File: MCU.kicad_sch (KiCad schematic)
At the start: 47 parts, among them J1 USB_C_Receptacle_USB2.0_16P, J2 DE9_Pins_MountingHoles, Q1 BC817, Q2 BC817, Q3 BC817, Q4 BC817, SW1 SW_SPST, SW2 SW_SPST, U1 W25Q128JVS, U2 ESP32-S3-MINI-1U, U3 MAX3232

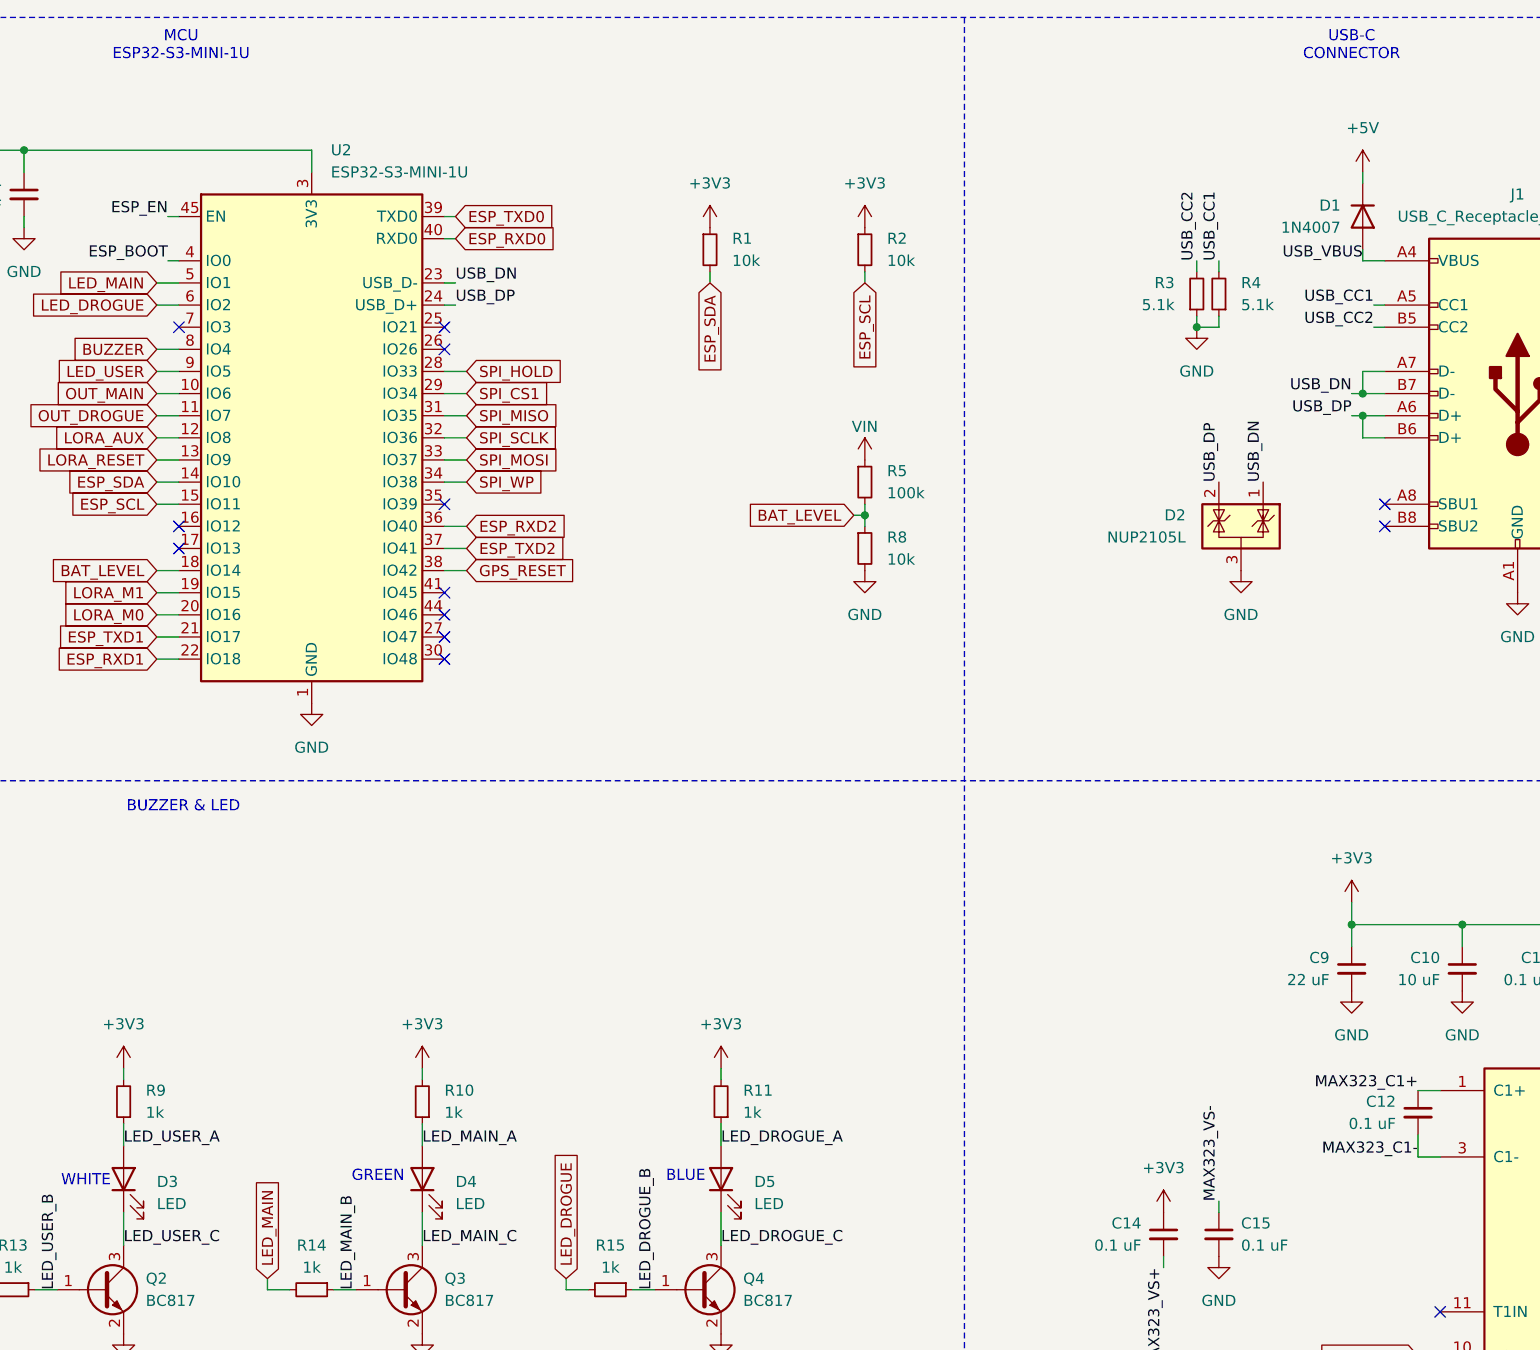
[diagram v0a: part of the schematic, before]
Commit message: Added more graphics, removed some unnecessary features. moved GPU passive components upper. added switching components to LoRa.
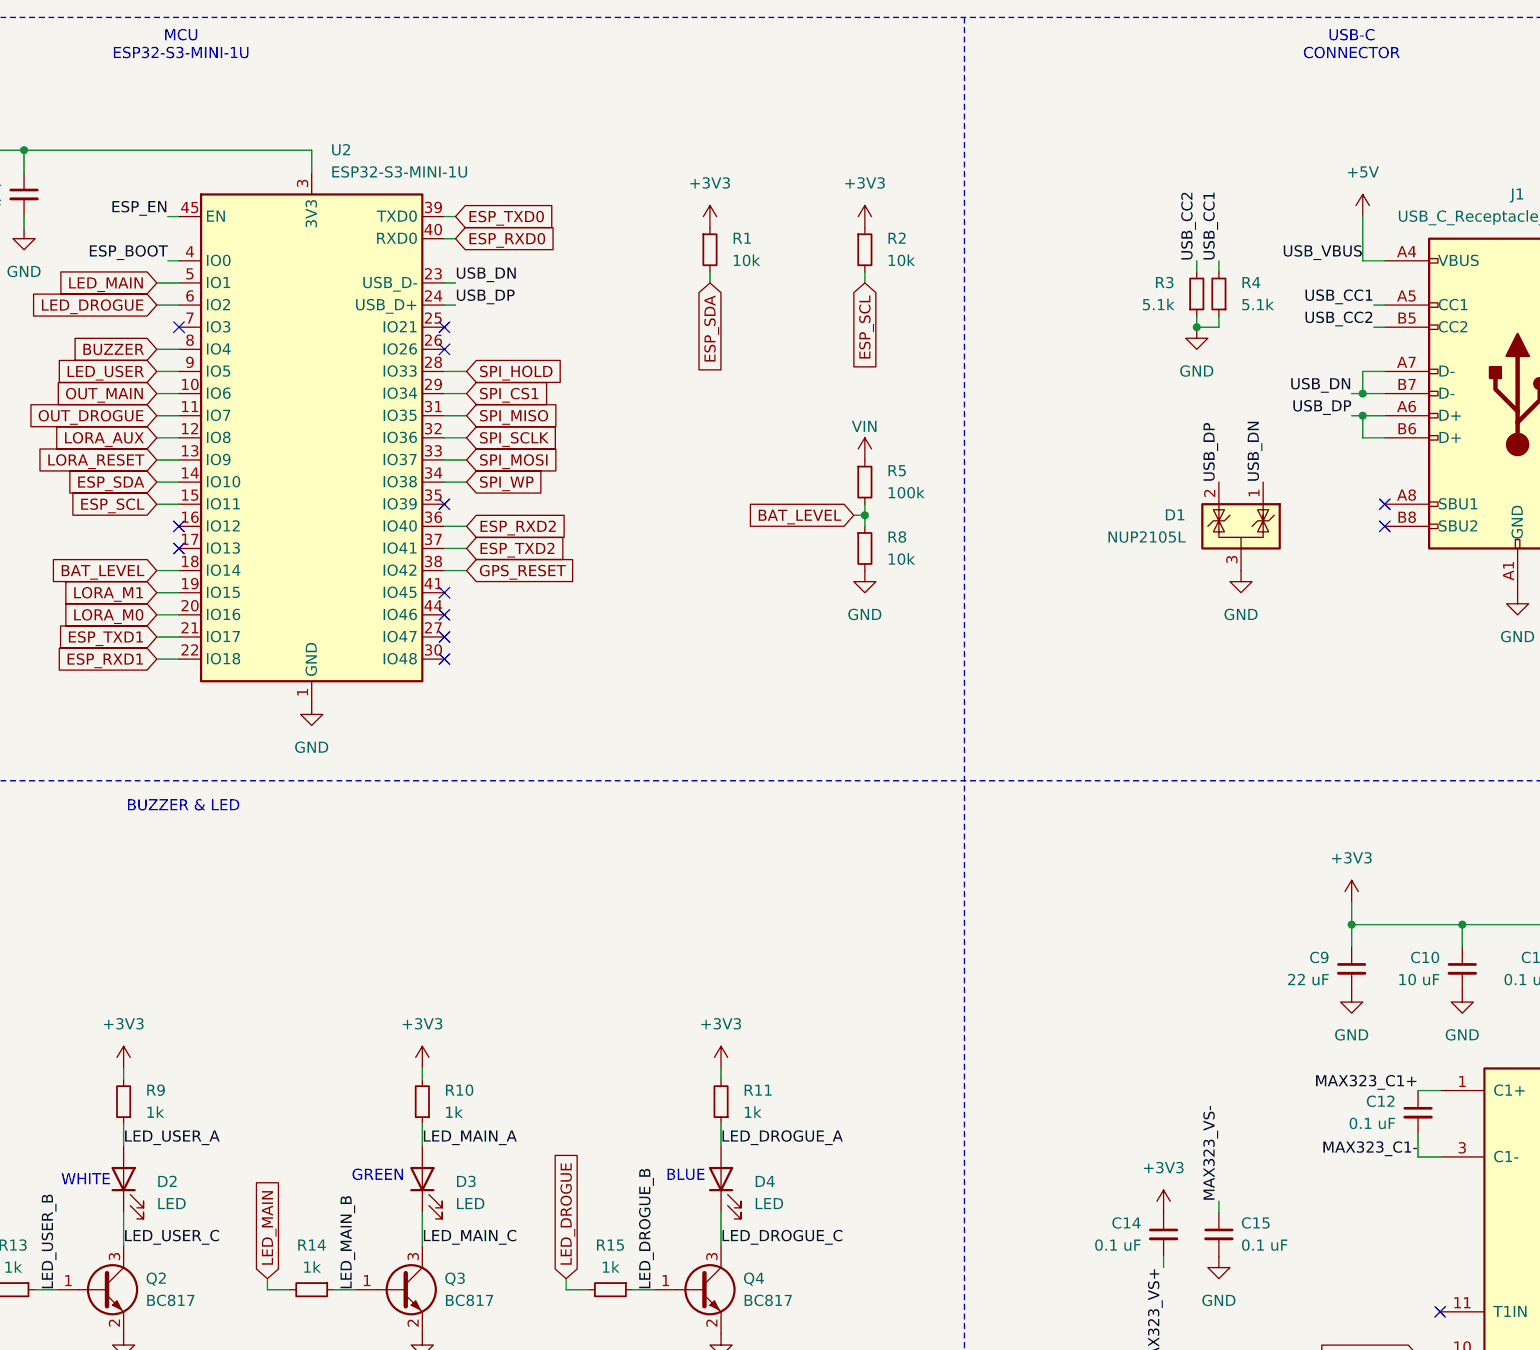
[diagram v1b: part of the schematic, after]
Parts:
- removed D1: 1N4007, Diode_THT:D_DO-41_SOD81_P2.54mm_Vertical_AnodeUp, symbol Diode:1N4007
- renumbered D2 to D1, D3 to D2, D4 to D3, D5 to D4
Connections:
- net USB_VBUS is gone; now on net +5V: J1.A4 (VBUS), J1.A9 (VBUS), J1.B4 (VBUS), J1.B9 (VBUS)
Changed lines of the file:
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@@
 	(wire
 		(pts
-			(xy 238.76 38.1) (xy 238.76 39.37)
-		)
-		(stroke
-			(width 0)
-			(type default)
-		)
-	)
-	(wire
-		(pts
 			(xy 100.33 86.36) (xy 102.87 86.36)
 		)
@@
 	(wire
 		(pts
-			(xy 238.76 48.26) (xy 238.76 46.99)
+			(xy 238.76 43.18) (xy 238.76 48.26)
 		)
 		(stroke
@@
 		(on_board yes)
 		(dnp no)
-		(property "Reference" "D2"
+		(property "Reference" "D1"
 			(at 218.44 77.4699 0)
 			(effects
@@
 			(project ""
 				(path "/d24fd15c-a242-4d26-9876-7755ca0d378c/d62cb9a5-57b0-46af-b3af-5759837aeb39"
-					(reference "D2")
+					(reference "D1")
 					(unit 1)
 				)
@@
 		(dnp no)
 		(fields_autoplaced yes)
-		(property "Reference" "D4"
+		(property "Reference" "D3"
 			(at 134.62 153.9874 90)
 			(effects
@@
 			(project "valkyriev3"
 				(path "/d24fd15c-a242-4d26-9876-7755ca0d378c/d62cb9a5-57b0-46af-b3af-5759837aeb39"
-					(reference "D4")
+					(reference "D3")
 					(unit 1)
 				)
@@
 	(symbol
 		(lib_id "power:+5V")
-		(at 238.76 38.1 0)
+		(at 238.76 43.18 0)
 		(unit 1)
 		(exclude_from_sim no)
@@
 		(fields_autoplaced yes)
 		(property "Reference" "#PWR02"
-			(at 238.76 41.91 0)
+			(at 238.76 46.99 0)
 			(effects
 				(font
@@
 		)
 		(property "Value" "+5V"
-			(at 238.76 33.02 0)
+			(at 238.76 38.1 0)
 			(effects
 				(font
@@
 		)
 		(property "Footprint" ""
-			(at 238.76 38.1 0)
+			(at 238.76 43.18 0)
 			(effects
 				(font
@@
 		)
 		(property "Datasheet" ""
-			(at 238.76 38.1 0)
+			(at 238.76 43.18 0)
 			(effects
 				(font
@@
 		)
 		(property "Description" "Power symbol creates a global label with name \"+5V\""
-			(at 238.76 38.1 0)
+			(at 238.76 43.18 0)
 			(effects
 				(font
@@
 	)
 	(symbol
-		(lib_id "Diode:1N4007")
-		(at 238.76 43.18 270)
-		(unit 1)
-		(exclude_from_sim no)
-		(in_bom yes)
-		(on_board yes)
-		(dnp no)
-		(property "Reference" "D1"
-			(at 236.22 41.9099 90)
-			(effects
-				(font
-					(size 1.27 1.27)
-				)
-				(justify right)
-			)
-		)
-		(property "Value" "1N4007"
-			(at 236.22 44.4499 90)
-			(effects
-				(font
-					(size 1.27 1.27)
-				)
-				(justify right)
-			)
-		)
-		(property "Footprint" "Diode_THT:D_DO-41_SOD81_P2.54mm_Vertical_AnodeUp"
-			(at 234.315 43.18 0)
-			(effects
-				(font
-					(size 1.27 1.27)
-				)
-				(hide yes)
-			)
-		)
-		(property "Datasheet" "http://www.vishay.com/docs/88503/1n4001.pdf"
-			(at 238.76 43.18 0)
-			(effects
-				(font
-					(size 1.27 1.27)
-				)
-				(hide yes)
-			)
-		)
-		(property "Description" "1000V 1A General Purpose Rectifier Diode, DO-41"
-			(at 238.76 43.18 0)
-			(effects
-				(font
-					(size 1.27 1.27)
-				)
-				(hide yes)
-			)
-		)
-		(property "Sim.Device" "D"
-			(at 238.76 43.18 0)
-			(effects
-				(font
-					(size 1.27 1.27)
-				)
-				(hide yes)
-			)
-		)
-		(property "Sim.Pins" "1=K 2=A"
-			(at 238.76 43.18 0)
-			(effects
-				(font
-					(size 1.27 1.27)
-				)
-				(hide yes)
-			)
-		)
-		(pin "2"
-		)
-		(pin "1"
-		)
-		(instances
-			(project ""
-				(path "/d24fd15c-a242-4d26-9876-7755ca0d378c/d62cb9a5-57b0-46af-b3af-5759837aeb39"
-					(reference "D1")
-					(unit 1)
-				)
-			)
-		)
-	)
-	(symbol
 		(lib_id "power:GND")
 		(at 59.69 171.45 0)
@@
 		(dnp no)
 		(fields_autoplaced yes)
-		(property "Reference" "D5"
+		(property "Reference" "D4"
 			(at 168.91 153.9874 90)
 			(effects
@@
 			(project "valkyriev3"
 				(path "/d24fd15c-a242-4d26-9876-7755ca0d378c/d62cb9a5-57b0-46af-b3af-5759837aeb39"
-					(reference "D5")
+					(reference "D4")
 					(unit 1)
 				)
@@
 		(dnp no)
 		(fields_autoplaced yes)
-		(property "Reference" "D3"
+		(property "Reference" "D2"
 			(at 100.33 153.9874 90)
 			(effects
@@
 			(project "valkyriev3"
 				(path "/d24fd15c-a242-4d26-9876-7755ca0d378c/d62cb9a5-57b0-46af-b3af-5759837aeb39"
-					(reference "D3")
+					(reference "D2")
 					(unit 1)
 				)
